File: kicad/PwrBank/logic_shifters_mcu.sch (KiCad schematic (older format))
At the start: 3 parts, among them Q4 BSS138

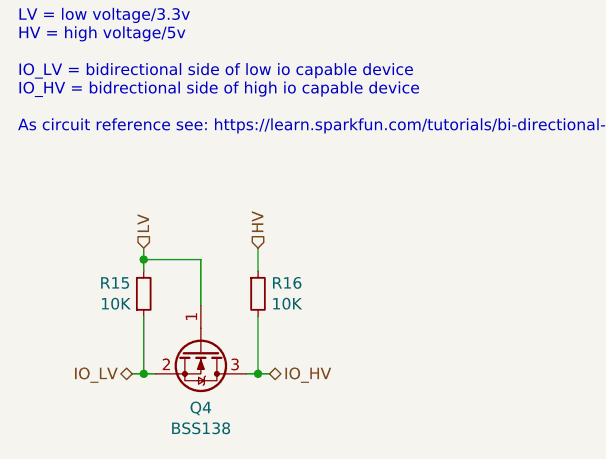
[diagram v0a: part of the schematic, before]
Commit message: Work on schematic+implement capacitive feature using TOUCH0
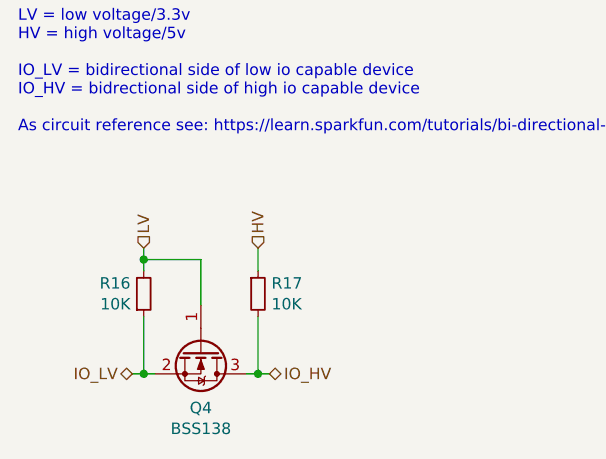
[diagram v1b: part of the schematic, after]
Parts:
- renumbered R15 to R16, R16 to R17
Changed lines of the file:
@@
 $Descr A4 11693 8268
 encoding utf-8
-Sheet 7 9
+Sheet 8 9
 Title "Logic Shifters MCU"
 Date "2021-07-17"
@@
 LV
 $Comp
-L Device:R_Small R15
+L Device:R_Small R16
 U 1 1 60F399FD
 P 3250 2500
-AR Path="/60F2D9E7/60F3980E/60F399FD" Ref="R15"  Part="1"
-AR Path="/60F2D9E7/60F56C27/60F399FD" Ref="R13"  Part="1"
-F 0 "R15" H 3192 2454 50  0000 R CNN
+AR Path="/60F2D9E7/60F3980E/60F399FD" Ref="R16"  Part="1"
+AR Path="/60F2D9E7/60F56C27/60F399FD" Ref="R14"  Part="1"
+F 0 "R16" H 3192 2454 50  0000 R CNN
 F 1 "10K" H 3192 2545 50  0000 R CNN
 F 2 "Resistor_SMD:R_0805_2012Metric_Pad1.20x1.40mm_HandSolder" H 3250 2500 50  0001 C CNN
@@
 $EndComp
 $Comp
-L Device:R_Small R16
+L Device:R_Small R17
 U 1 1 60F39B1A
 P 3750 2500
-AR Path="/60F2D9E7/60F3980E/60F39B1A" Ref="R16"  Part="1"
-AR Path="/60F2D9E7/60F56C27/60F39B1A" Ref="R14"  Part="1"
-F 0 "R16" H 3809 2546 50  0000 L CNN
+AR Path="/60F2D9E7/60F3980E/60F39B1A" Ref="R17"  Part="1"
+AR Path="/60F2D9E7/60F56C27/60F39B1A" Ref="R15"  Part="1"
+F 0 "R17" H 3809 2546 50  0000 L CNN
 F 1 "10K" H 3809 2455 50  0000 L CNN
 F 2 "Resistor_SMD:R_0805_2012Metric_Pad1.20x1.40mm_HandSolder" H 3750 2500 50  0001 C CNN
